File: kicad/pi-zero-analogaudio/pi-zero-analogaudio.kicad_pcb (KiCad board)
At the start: 2 copper layers, 38 x 26 mm, 11 parts, among them J1 AudioJack3, J2 Pi Connector 2x5 Female, J3 Audio-Out

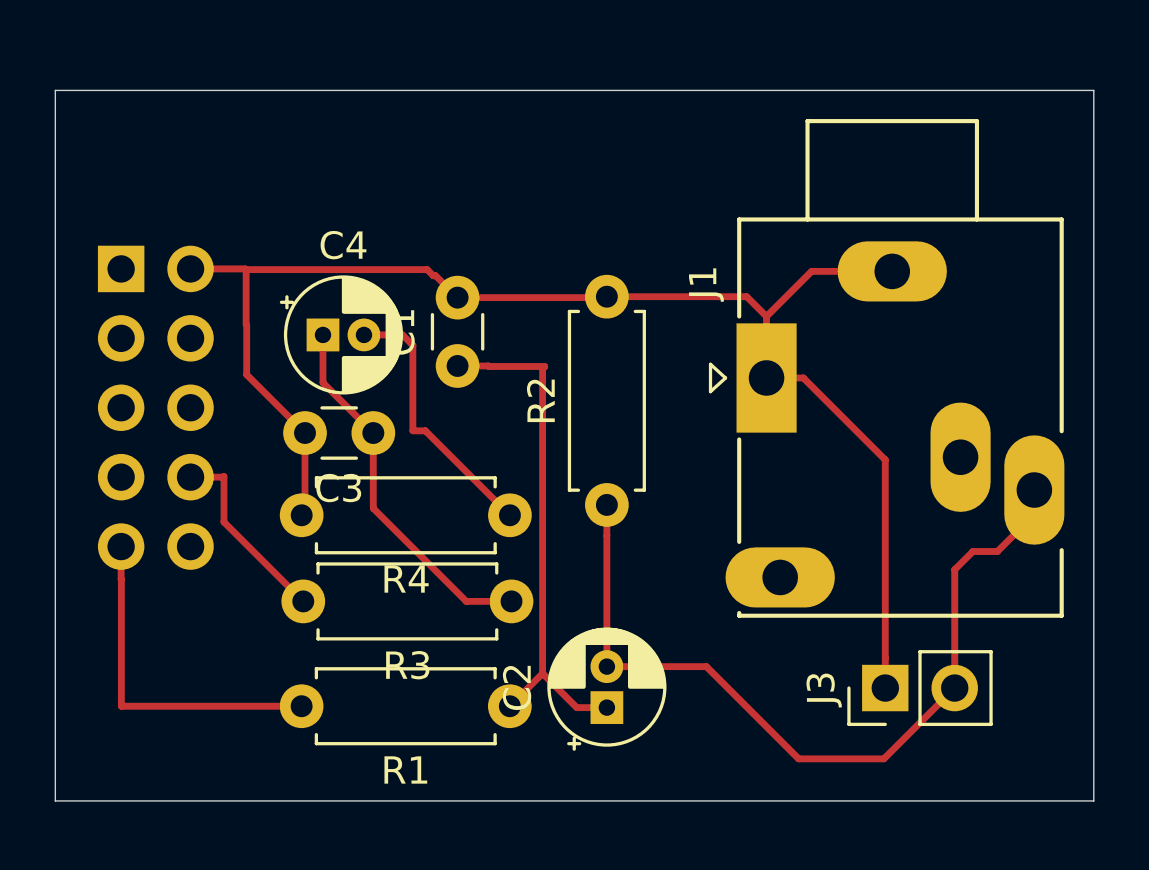
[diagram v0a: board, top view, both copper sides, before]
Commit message: fixed wrong connection for R4
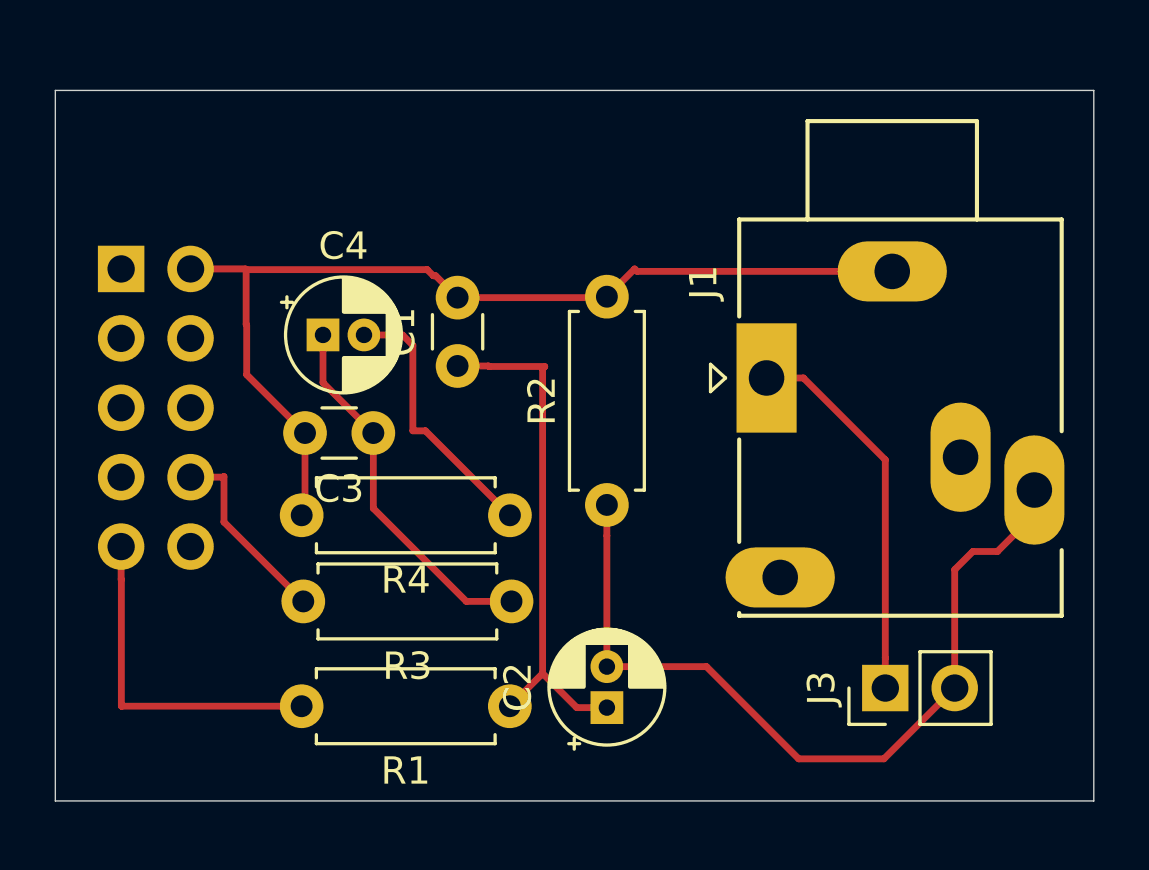
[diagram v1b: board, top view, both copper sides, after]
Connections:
- J1 pad T: Net-(C1-Pad2) -> Net-(C4-Pad2)
- J3 pad 1: Net-(C1-Pad2) -> Net-(C4-Pad2)
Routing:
- net Net-(C1-Pad2): track 53.2 -> 36.5 mm
- net Net-(C4-Pad2): track 9.96 -> 23.9 mm
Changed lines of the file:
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@@
     (thickness 1.6)
     (drawings 4)
-    (tracks 62)
+    (tracks 60)
     (zones 0)
     (modules 11)
@@
     (fp_circle (center 0.1 -1.75) (end 0.4 -1.55) (layer F.Fab) (width 0.12))
     (pad T thru_hole rect (at 0 0 270) (size 4 2.2) (drill 1.3) (layers *.Cu *.Mask)
-      (net 2 "Net-(C1-Pad2)"))
+      (net 5 "Net-(C4-Pad2)"))
     (pad TN thru_hole oval (at 7.3 -0.5) (size 4 2.2) (drill 1.3) (layers *.Cu *.Mask))
     (pad RN thru_hole oval (at 2.9 -7.1 270) (size 4 2.2) (drill 1.3) (layers *.Cu *.Mask))
@@
     )
     (pad 1 thru_hole rect (at 0 0 90) (size 1.7 1.7) (drill 1) (layers *.Cu *.Mask)
-      (net 2 "Net-(C1-Pad2)"))
+      (net 5 "Net-(C4-Pad2)"))
     (pad 2 thru_hole oval (at 0 2.54 90) (size 1.7 1.7) (drill 1) (layers *.Cu *.Mask)
       (net 3 "Net-(C2-Pad2)"))
@@
   (segment (start 107.148 66.58292) (end 107.18292 66.548) (width 0.25) (layer F.Cu) (net 2))
   (segment (start 101.71938 66.58292) (end 107.148 66.58292) (width 0.25) (layer F.Cu) (net 2))
-  (segment (start 112.30058 66.548) (end 113.02492 67.27234) (width 0.25) (layer F.Cu) (net 2))
-  (segment (start 107.18292 66.548) (end 112.30058 66.548) (width 0.25) (layer F.Cu) (net 2))
-  (segment (start 113.02492 69.52234) (end 113.02492 67.27234) (width 0.25) (layer F.Cu) (net 2))
-  (segment (start 114.67492 65.62234) (end 117.62492 65.62234) (width 0.25) (layer F.Cu) (net 2))
-  (segment (start 113.02492 67.27234) (end 114.67492 65.62234) (width 0.25) (layer F.Cu) (net 2))
-  (segment (start 117.37086 72.51828) (end 117.37086 79.76852) (width 0.25) (layer F.Cu) (net 2))
-  (segment (start 117.37086 79.76852) (end 117.37086 80.86852) (width 0.25) (layer F.Cu) (net 2))
-  (segment (start 114.37492 69.52234) (end 117.37086 72.51828) (width 0.25) (layer F.Cu) (net 2))
-  (segment (start 113.02492 69.52234) (end 114.37492 69.52234) (width 0.25) (layer F.Cu) (net 2))
+  (segment (start 107.18292 66.548) (end 108.19892 65.532) (width 0.25) (layer F.Cu) (net 2))
+  (segment (start 108.28926 65.62234) (end 117.62492 65.62234) (width 0.25) (layer F.Cu) (net 2))
+  (segment (start 108.19892 65.532) (end 108.28926 65.62234) (width 0.25) (layer F.Cu) (net 2))
+  (segment (start 117.37086 72.51828) (end 117.37086 79.76852) (width 0.25) (layer F.Cu) (net 5))
+  (segment (start 117.37086 79.76852) (end 117.37086 80.86852) (width 0.25) (layer F.Cu) (net 5))
+  (segment (start 114.37492 69.52234) (end 117.37086 72.51828) (width 0.25) (layer F.Cu) (net 5))
+  (segment (start 113.02492 69.52234) (end 114.37492 69.52234) (width 0.25) (layer F.Cu) (net 5))
   (segment (start 107.18292 75.29937) (end 107.18292 80.0848) (width 0.25) (layer F.Cu) (net 3))
   (segment (start 107.18292 74.168) (end 107.18292 75.29937) (width 0.25) (layer F.Cu) (net 3))

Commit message: updated pcb for revision 5
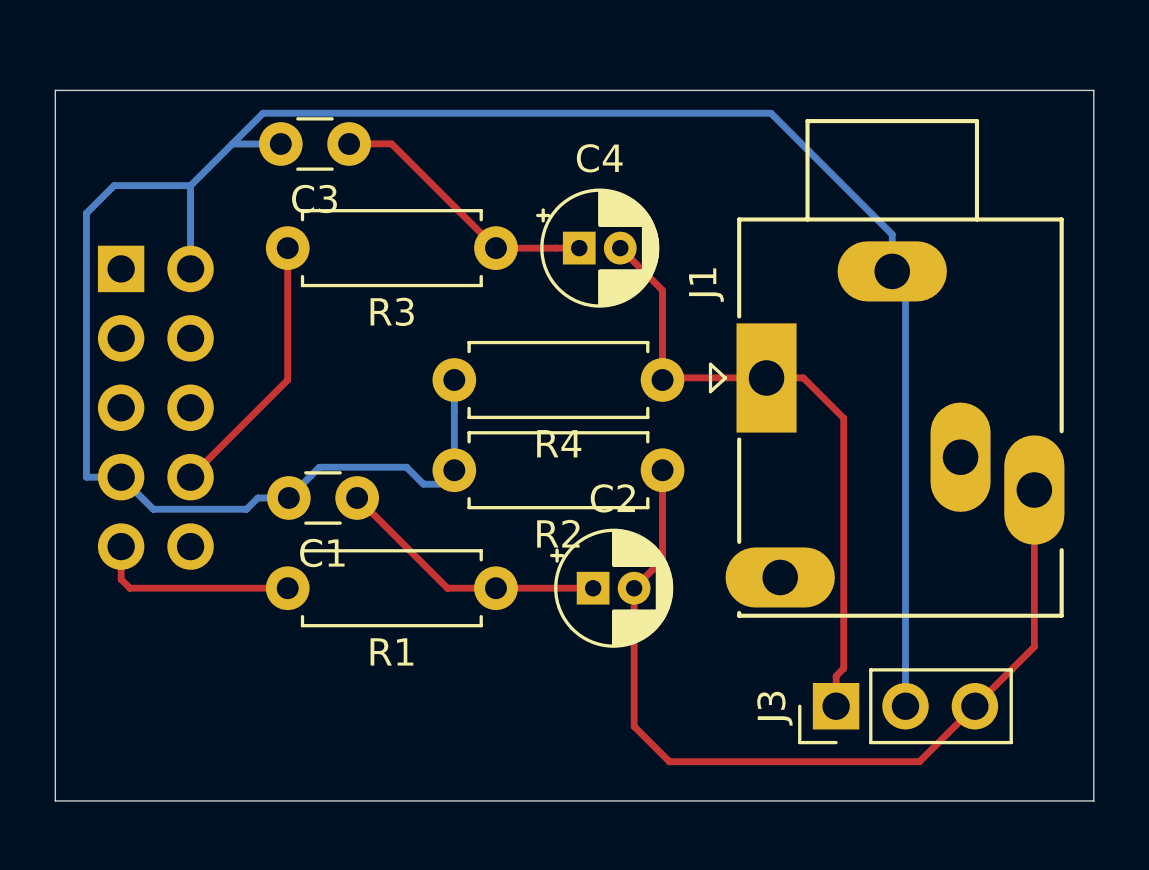
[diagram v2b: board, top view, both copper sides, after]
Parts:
- J3: value Audio-Out -> Audio Out; footprint Connector_PinHeader_2.54mm:PinHeader_1x02_P2.54mm_Vertical -> Connector_PinHeader_2.54mm:PinHeader_1x03_P2.54mm_Vertical
- moved R3 12.9 mm to (103.1, 64.8)
- moved C3 10.6 mm to (97.8, 61.0)
- moved C4 9.90 mm to (106.2, 64.8)
- moved R4 7.46 mm to (109.2, 69.6)
- moved C1 6.07 mm to (98.0, 73.9), turned to 180 degrees
- moved C2 4.40 mm to (106.7, 77.2), turned to 0 degrees
- moved R1 4.35 mm to (103.1, 77.2)
- moved R2 2.40 mm to (109.2, 72.9), turned to 180 degrees
- moved J3 1.92 mm to (115.6, 81.5)
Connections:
- J2 pad 7: Net-(J2-Pad7) -> Net-(C1-Pad2)
- J3 pad 2: Net-(C2-Pad2) -> Net-(C1-Pad2)
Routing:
- net Net-(C1-Pad2): track 36.5 -> 83.4 mm
- net Net-(C1-Pad1): track 19.0 -> 10.0 mm
- net Net-(J2-Pad9): track 12.4 -> 7.43 mm
- net Net-(C3-Pad1): track 13.6 -> 10.0 mm
- net Net-(J2-Pad8): track 7.00 -> 9.85 mm
- net Net-(C2-Pad2): track 30.1 -> 32.0 mm
- net Net-(C4-Pad2): track 23.9 -> 23.4 mm

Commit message: updated layout (size, components)
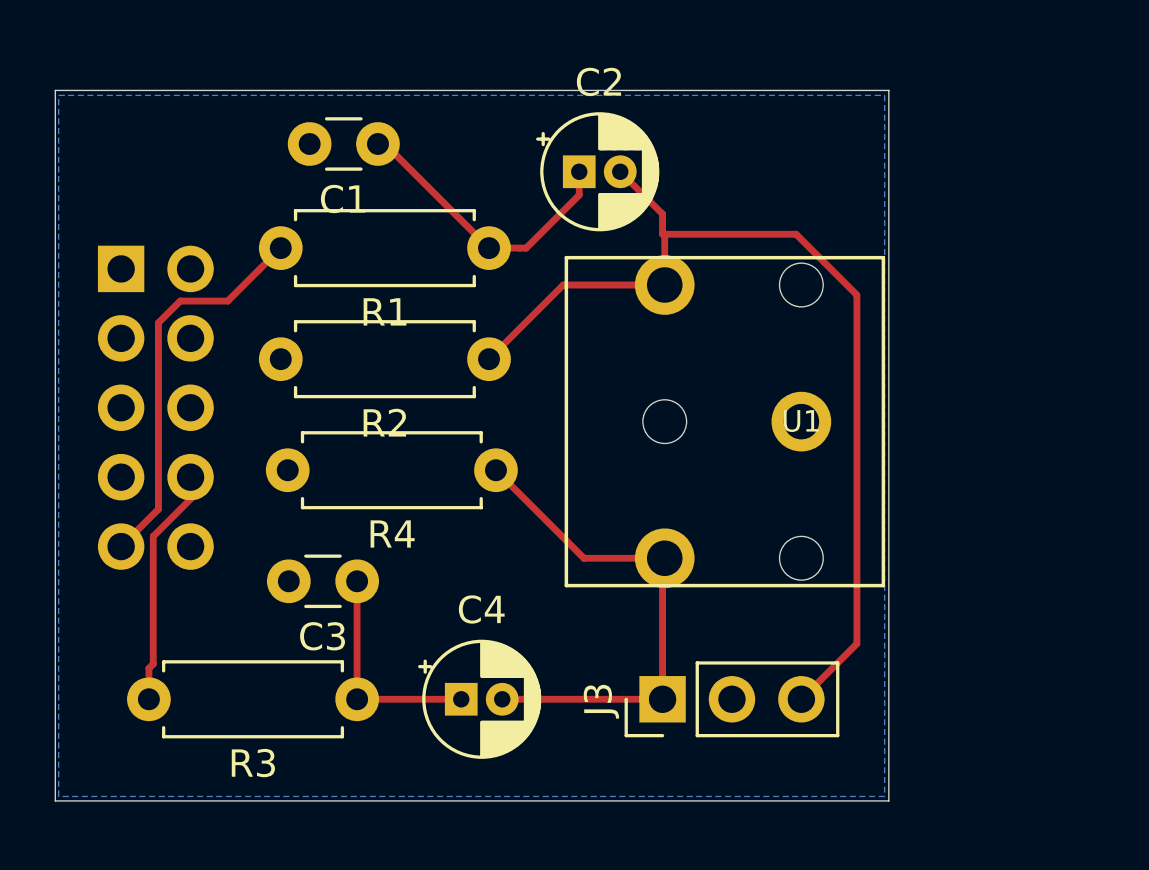
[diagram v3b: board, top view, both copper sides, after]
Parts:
- removed J1: AudioJack3, Connector_Audio:Jack_3.5mm_Ledino_KB3SPRS_Horizontal
- added U1: STX-3120-3B, STX-3120, F.Cu at (114.3, 71.1)
- moved R3 17.3 mm to (98.0, 81.3)
- moved C4 17.1 mm to (101.9, 81.3)
- moved C3 16.0 mm to (98.0, 77.0)
- moved C2 15.2 mm to (106.2, 62.0)
- moved C1 13.0 mm to (98.8, 61.0)
- moved R1 12.4 mm to (102.9, 64.8)
- moved R2 7.54 mm to (102.9, 68.8)
- moved R4 6.93 mm to (103.1, 72.9)
- moved J3 6.36 mm to (109.2, 81.3)
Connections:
- net Net-(C1-Pad2) renamed GND
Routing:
- net GND: track 83.4 -> 0.00 mm
- net Net-(J2-Pad9): track 7.43 -> 14.4 mm
- net Net-(C4-Pad2): track 23.4 -> 18.6 mm
- net Net-(C2-Pad2): track 32.0 -> 36.0 mm
- net Net-(C3-Pad1): track 10.0 -> 8.13 mm
- net Net-(J2-Pad8): track 9.85 -> 8.76 mm
- net Net-(C1-Pad1): track 10.0 -> 10.6 mm
- added copper zone on B.Cu, net GND
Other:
- board size 38 x 26 mm -> 30.5 x 26 mm

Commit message: slightly moved header to (hopefully) fit hat-dimensions
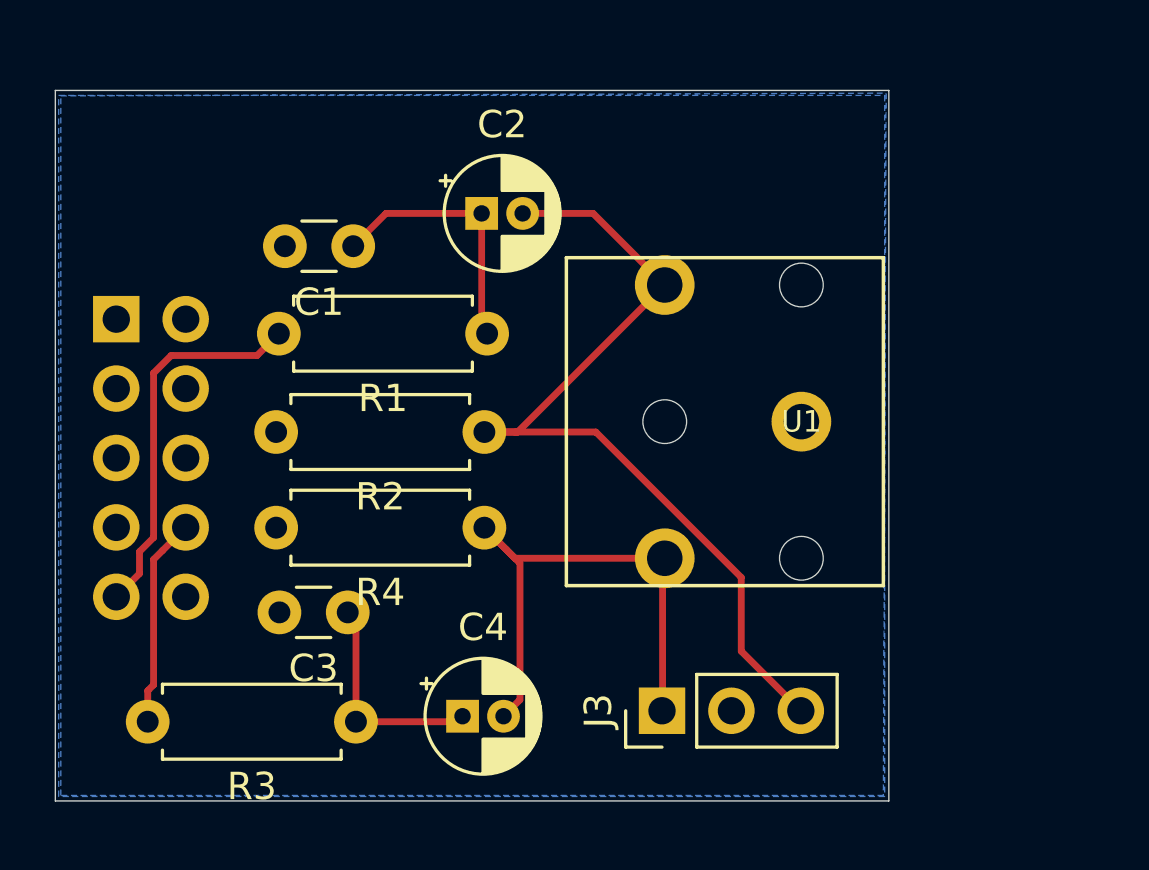
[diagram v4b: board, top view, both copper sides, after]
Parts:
- moved C2 3.88 mm to (102.6, 63.5)
- moved C1 3.85 mm to (97.9, 64.7)
- moved R1 3.13 mm to (102.8, 67.9)
- moved R2 2.67 mm to (102.7, 71.5)
- moved R4 2.14 mm to (102.7, 75.0)
- moved J2 1.85 mm to (89.2, 67.4)
- moved C3 1.19 mm to (97.7, 78.1)
- moved R3 0.82 mm to (98.0, 82.1)
- moved C4 0.62 mm to (101.9, 81.9)
- moved J3 0.42 mm to (109.2, 81.7)
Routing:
- net Net-(C2-Pad2): track 36.0 -> 32.5 mm
- net Net-(C4-Pad2): track 18.6 -> 19.9 mm
- net Net-(J2-Pad8): track 8.76 -> 7.69 mm
- net Net-(C1-Pad1): track 10.6 -> 9.68 mm
